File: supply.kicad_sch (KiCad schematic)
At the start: 23 parts, among them IC3 BQ25622ERYKR, IC4 BQ27427YZFR, IC7 TPS62291DRVR, IC8 TPS62293DRVR

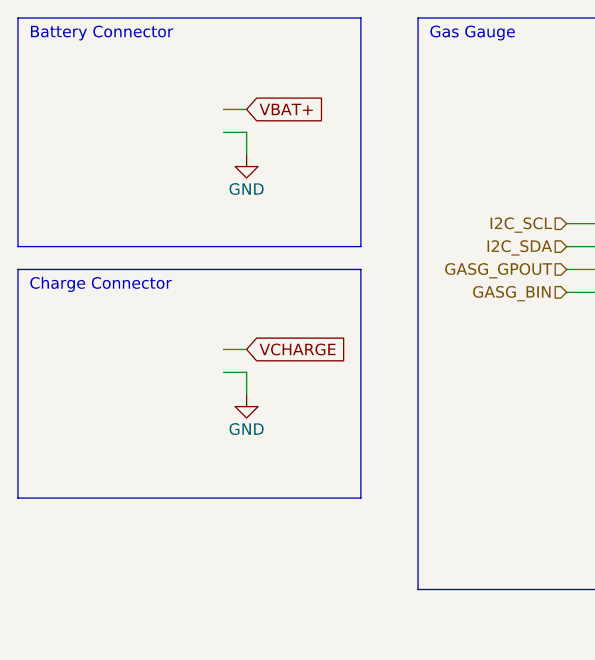
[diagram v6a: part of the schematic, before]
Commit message: added usb connector
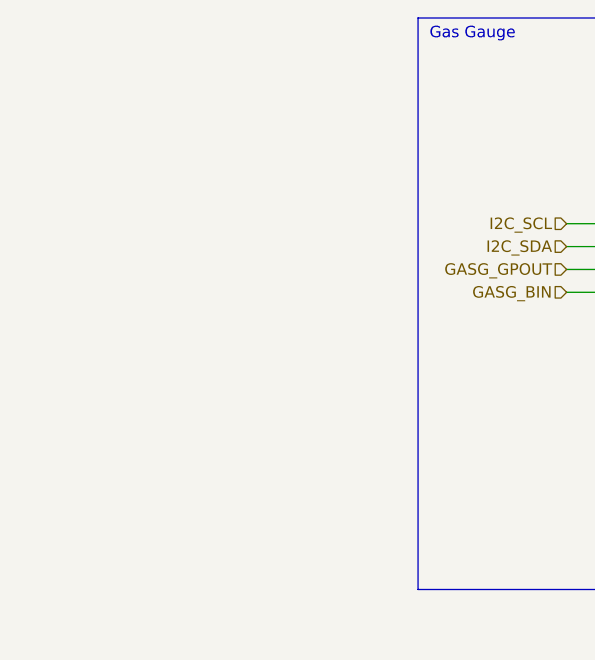
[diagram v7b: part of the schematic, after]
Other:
- note removed: "Battery Connector"
- note removed: "Charge Connector"
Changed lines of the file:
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@@
-    (stroke (width 0) (type default))
-  )
-  (polyline (pts (xy 25.4 25.4) (xy 25.4 50.8))
     (stroke (width 0) (type default))
   )
@@
     (stroke (width 0) (type default))
   )
-  (wire (pts (xy 50.8 67.31) (xy 50.8 64.77))
-    (stroke (width 0) (type default))
-  )
   (wire (pts (xy 46.99 166.37) (xy 46.99 168.91))
     (stroke (width 0) (type default))
@@
     (stroke (width 0) (type default))
   )
-  (polyline (pts (xy 63.5 53.34) (xy 25.4 53.34))
-    (stroke (width 0) (type default))
-  )
   (wire (pts (xy 240.03 40.64) (xy 245.11 40.64))
     (stroke (width 0) (type default))
@@
     (stroke (width 0) (type default))
   )
-  (wire (pts (xy 48.26 62.23) (xy 50.8 62.23))
-    (stroke (width 0) (type default))
-  )
   (wire (pts (xy 110.49 129.54) (xy 110.49 132.08))
     (stroke (width 0) (type default))
   )
-  (polyline (pts (xy 63.5 53.34) (xy 63.5 78.74))
-    (stroke (width 0) (type default))
-  )
-  (wire (pts (xy 50.8 40.64) (xy 50.8 38.1))
-    (stroke (width 0) (type default))
-  )
   (wire (pts (xy 198.12 58.42) (xy 200.66 58.42))
     (stroke (width 0) (type default))
@@
     (stroke (width 0) (type default))
   )
-  (polyline (pts (xy 63.5 25.4) (xy 63.5 50.8))
-    (stroke (width 0) (type default))
-  )
   (wire (pts (xy 184.15 40.64) (xy 200.66 40.64))
     (stroke (width 0) (type default))
@@
     (stroke (width 0) (type default))
   )
-  (wire (pts (xy 48.26 35.56) (xy 50.8 35.56))
-    (stroke (width 0) (type default))
-  )
   (wire (pts (xy 184.15 41.91) (xy 184.15 40.64))
     (stroke (width 0) (type default))
@@
     (stroke (width 0) (type default))
   )
-  (polyline (pts (xy 63.5 25.4) (xy 25.4 25.4))
-    (stroke (width 0) (type default))
-  )
   (wire (pts (xy 104.14 123.19) (xy 110.49 123.19))
     (stroke (width 0) (type default))
@@
     (stroke (width 0) (type default))
   )
-  (polyline (pts (xy 25.4 50.8) (xy 63.5 50.8))
-    (stroke (width 0) (type default))
-  )
   (wire (pts (xy 60.96 123.19) (xy 63.5 123.19))
     (stroke (width 0) (type default))
@@
     (stroke (width 0) (type default))
   )
-  (polyline (pts (xy 25.4 78.74) (xy 63.5 78.74))
-    (stroke (width 0) (type default))
-  )
   (wire (pts (xy 264.16 58.42) (xy 266.7 58.42))
     (stroke (width 0) (type default))
@@
     (stroke (width 0) (type default))
   )
-  (wire (pts (xy 48.26 64.77) (xy 50.8 64.77))
-    (stroke (width 0) (type default))
-  )
-  (polyline (pts (xy 25.4 53.34) (xy 25.4 78.74))
-    (stroke (width 0) (type default))
-  )
   (wire (pts (xy 86.36 50.8) (xy 91.44 50.8))
     (stroke (width 0) (type default))
@@
     (stroke (width 0) (type default))
   )
-  (wire (pts (xy 48.26 38.1) (xy 50.8 38.1))
-    (stroke (width 0) (type default))
-  )
   (wire (pts (xy 193.04 78.74) (xy 200.66 78.74))
     (stroke (width 0) (type default))
@@
     (stroke (width 0) (type default))
     (fill (type none))
-  )
-  (text "Battery Connector" (at 26.67 27.94 0)
-    (effects (font (size 1.27 1.27)) (justify left bottom))
-  )
-  (text "Charge Connector" (at 26.67 55.88 0)
-    (effects (font (size 1.27 1.27)) (justify left bottom))
   )
   (text "Gas Gauge" (at 71.12 27.94 0)
@@
     (property "Intersheetrefs" "${INTERSHEET_REFS}" (at 167.6975 40.64 0)
       (effects (font (size 1.27 1.27)) (justify right) hide)
-    )
-  )
-  (global_label "VCHARGE" (shape input) (at 50.8 62.23 0) (fields_autoplaced)
-    (effects (font (size 1.27 1.27)) (justify left))
-    (property "Intersheetrefs" "${INTERSHEET_REFS}" (at 62.1725 62.23 0)
-      (effects (font (size 1.27 1.27)) (justify left) hide)
-    )
-  )
-  (global_label "VBAT+" (shape input) (at 50.8 35.56 0) (fields_autoplaced)
-    (effects (font (size 1.27 1.27)) (justify left))
-    (property "Intersheetrefs" "${INTERSHEET_REFS}" (at 59.693 35.56 0)
-      (effects (font (size 1.27 1.27)) (justify left) hide)
     )
   )
@@
         )
       )
-    )
-  )
-  (symbol (lib_id "power:GND") (at 50.8 40.64 0) (unit 1)
-    (in_bom yes) (on_board yes) (dnp no)
-    (property "Reference" "#PWR01" (at 50.8 46.99 0)
-      (effects (font (size 1.27 1.27)) hide)
-    )
-    (property "Value" "GND" (at 50.8 44.45 0)
-      (effects (font (size 1.27 1.27)))
-    )
-    (property "Footprint" "" (at 50.8 40.64 0)
-      (effects (font (size 1.27 1.27)) hide)
-    )
-    (property "Datasheet" "" (at 50.8 40.64 0)
-      (effects (font (size 1.27 1.27)) hide)
-    )
-    (pin "1")
-    (instances
-      (project "armband"
-        (path "/017c50c6-333c-4d31-ad5a-278994a09b14"
-          (reference "#PWR01") (unit 1)
-        )
-        (path "/017c50c6-333c-4d31-ad5a-278994a09b14/ae5dc462-dca9-40e4-ba02-6b87a86a4904"
-          (reference "#PWR021") (unit 1)
-        )
-      )
-    )
-  )
-  (symbol (lib_id "power:GND") (at 50.8 67.31 0) (unit 1)
-    (in_bom yes) (on_board yes) (dnp no)
-    (property "Reference" "#PWR01" (at 50.8 73.66 0)
-      (effects (font (size 1.27 1.27)) hide)
-    )
-    (property "Value" "GND" (at 50.8 71.12 0)
-      (effects (font (size 1.27 1.27)))
-    )
-    (property "Footprint" "" (at 50.8 67.31 0)
-      (effects (font (size 1.27 1.27)) hide)
-    )
-    (property "Datasheet" "" (at 50.8 67.31 0)
-      (effects (font (size 1.27 1.27)) hide)
-    )
-    (pin "1")
-    (instances
-      (project "armband"
-        (path "/017c50c6-333c-4d31-ad5a-278994a09b14"
-          (reference "#PWR01") (unit 1)
-        )
-        (path "/017c50c6-333c-4d31-ad5a-278994a09b14/ae5dc462-dca9-40e4-ba02-6b87a86a4904"
-          (reference "#PWR022") (unit 1)
-        )
-      )

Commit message: finished usb connection ciruits
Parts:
- added J5: Conn_01x02, symbol Connector_Generic:Conn_01x02
- C8: value 0u1 -> 100n 16V; footprint (none) -> Capacitor_SMD:C_0402_1005Metric; MFN (none) -> 80-C0402C104M4V
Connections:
- net EP: now also J5.2 (Pin_2)
- net VBAT+: now also J5.1 (Pin_1)
- net VCHARGE renamed VUSB
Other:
- note added: "Battery Connector"
- note added: "TODO: footprint"
- moved on the sheet: C8, IC3, IC4, IC7, IC8, L1, L3, L4, R11, R12, R13
